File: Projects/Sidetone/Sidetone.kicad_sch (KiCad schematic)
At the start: 53 parts, among them Q1 2N3904, Q2 2N3904, Q3 2N3904, SW1 morse key, SW2 On/off, U1 4N35, U2 LM324, U3 LM386

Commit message: 20240216
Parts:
- C1, C10, C11, C12, C13, C14, C2, C3, C4, C5, C6, C7, C8, C9: footprint Capacitor_THT:CP_Radial_D8.0mm_P3.80mm -> (none)
- R1, R10, R11, R12, R13, R14, R15, R16, R17, R18, R19, R2, R20, R21, R22, R23, R24, R3, R4, R5, R6, R7, R8, R9: footprint Resistor_THT:R_Axial_DIN0207_L6.3mm_D2.5mm_P7.62mm_Horizontal -> (none)

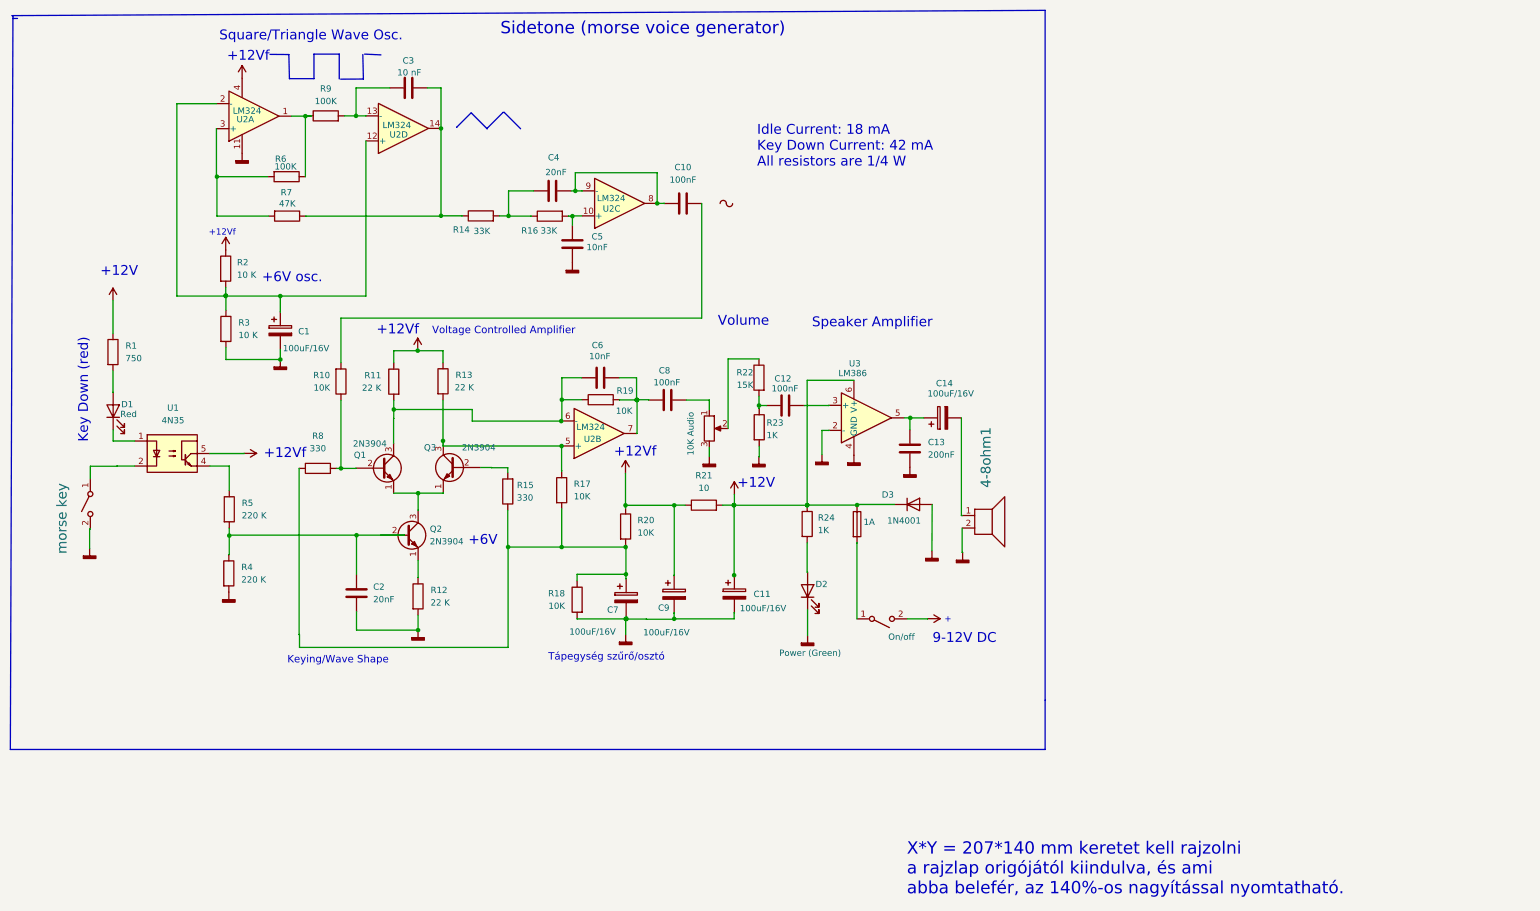
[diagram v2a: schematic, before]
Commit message: modified sidetone schematic
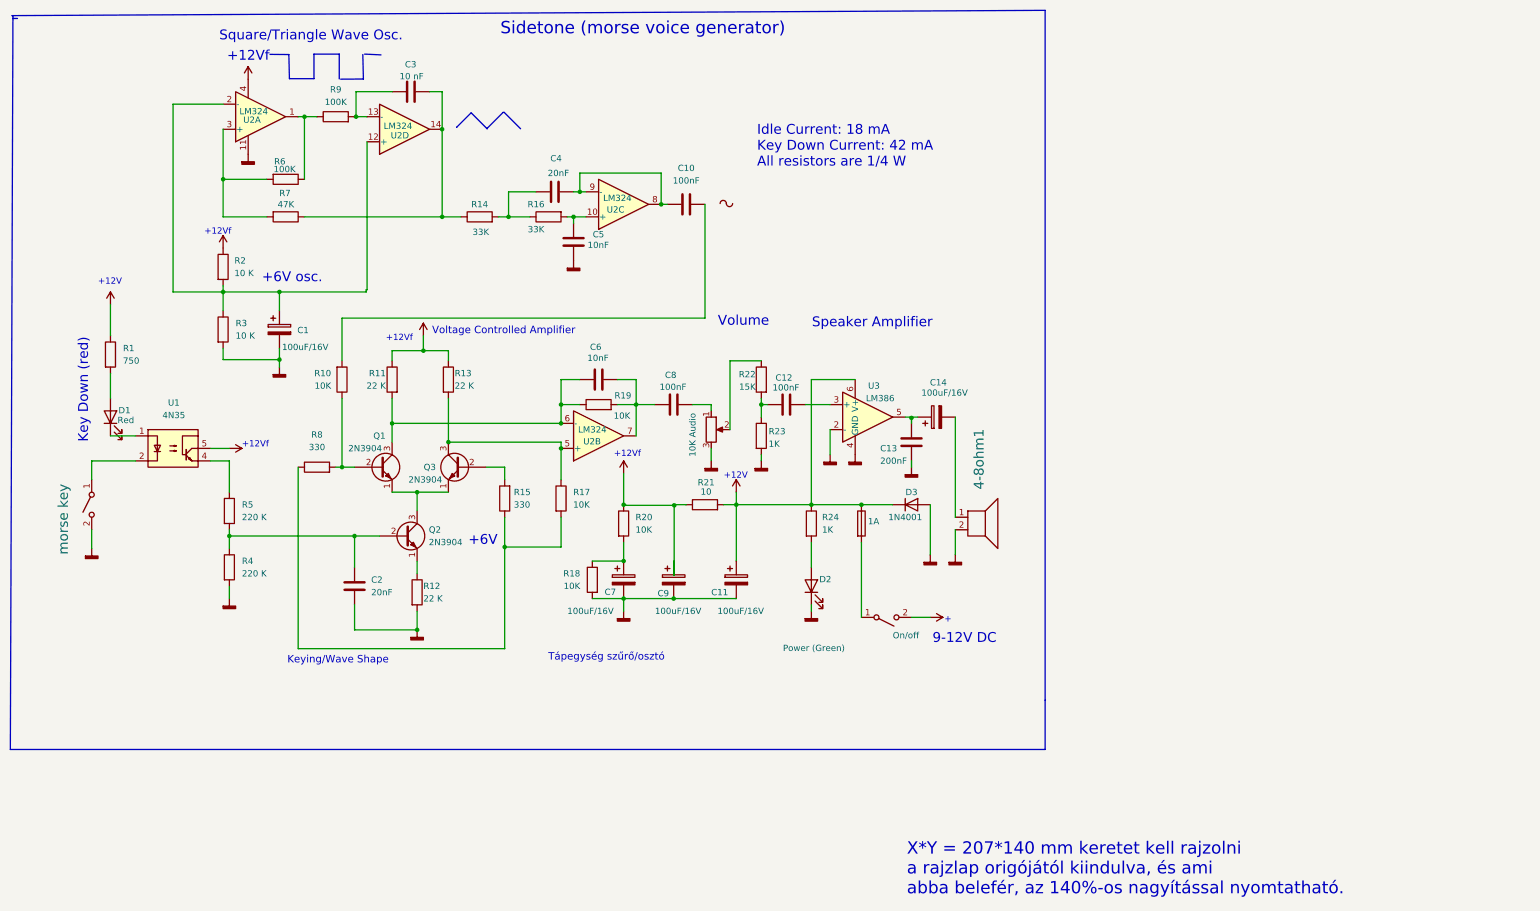
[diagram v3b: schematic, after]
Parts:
- 4-8ohm1: footprint (none) -> 000_Other_Device:Hangszoro
- C1, C11, C14, C7, C9: footprint (none) -> 000_Capacitor:CP_Radial_Elektrolit_D8.0mm_P4.0mm_H12
- C10, C12, C13, C2, C3, C4, C5, C6, C8: footprint (none) -> 000_Capacitor:C_Radial_Ceramic_D4.5mm_P5.00mm
- D1, D2: footprint (none) -> 000_Diode:LED_D5.0mm_P5.0_Clear
- D3: footprint Diode_THT:D_DO-41_SOD81_P10.16mm_Horizontal -> 000_Resistor:R_Axial_L6.3mm_D2.5mm_P10.0mm_Horizontal
- F1: footprint Fuse:Fuse_Littelfuse-LVR125 -> 000_Other_Device:Fuseholder_22x10mm_Horizontal
- Q1, Q2, Q3: footprint Package_TO_SOT_THT:TO-92_Inline -> 000_Resistor:R_Axial_L6.3mm_D2.5mm_P10.0mm_Horizontal
- R1, R10, R11, R12, R13, R14, R15, R16, R17, R18, R19, R2, R20, R21, R22, R23, R24, R3, R4, R5, R6, R7, R8, R9: footprint (none) -> 000_Resistor:R_Axial_L6.3mm_D2.5mm_P10.0mm_Horizontal
- RV1: footprint Potentiometer_THT:Potentiometer_Alps_RK09K_Single_Horizontal -> 000_Resistor:Potenciometer_4Pin_P7mm
- SW1: footprint (none) -> 000_Other_Device:Morse_Key_Pad_Group_2Pin_P7mm
- SW2: footprint (none) -> 000_Other_Device:Kapcsolo_Pad_Group_2Pin_P7mm
- U1: footprint Package_DIP:DIP-6_W7.62mm_Socket_LongPads -> 000_IC:DIP-6_W7.62mm_LongPads
- U2: footprint 001_user_library:DIP-14_296_ELL_LM324 -> 000_IC:DIP-14_LM324
- U3: footprint Package_DIP:DIP-6_W7.62mm_LongPads -> 000_IC:DIP-8_W7.62mm_Socket_LongPads
- V1: footprint 001_user_library:DIP-14_296_ELL_LM324 -> (none)
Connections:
- net at C7.1, R18.1, R20.2: no longer R15.1, R17.2, R8.1
- new net: R15.1, R17.2, R8.1
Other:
- moved on the sheet: 4-8ohm1, C10, C11, C13, C14, C2, C3, C4, C6, C7, C8, C9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

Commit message: 18-2
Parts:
- removed V1: VSIN, symbol Simulation_SPICE:VSIN
- Q1, Q2, Q3: footprint 000_Resistor:R_Axial_L6.3mm_D2.5mm_P10.0mm_Horizontal -> 000_Transistor:TO-92_Kis_Muanyag_Hazas_Transistor

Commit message: 20240222
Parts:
- added GND1: ~, 000_Other_Device:GND, symbol 000_Device:GND
- added Vcc1: ~, 000_Other_Device:+Vcc, symbol 000_Device:Vcc
- renumbered R5 to R4, R4 to R5
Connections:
- net GNDD: now also GND1. (GND)
- net VCC: now also Vcc1.
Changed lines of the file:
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@@
+    (stroke (width 0) (type default))
+  )
+  (wire (pts (xy 147.32 100.33) (xy 162.56 100.33))
     (stroke (width 0) (type default))
   )
@@
     (stroke (width 0) (type default))
   )
+  (wire (pts (xy 186.69 100.33) (xy 186.69 110.49))
+    (stroke (width 0) (type default))
+  )
   (polyline (pts (xy 158.934 42.4225) (xy 160.8121 42.4523))
     (stroke (width 0) (type default))
@@
   )
   (polyline (pts (xy 96.7546 23.9506) (xy 99.9939 20.7113))
-    (stroke (width 0) (type default))
-  )
-  (wire (pts (xy 147.32 100.33) (xy 162.56 100.33))
     (stroke (width 0) (type default))
   )
@@
   )
   (polyline (pts (xy 56.5208 8.9674) (xy 56.6364 13.8676))
-    (stroke (width 0) (type default))
-  )
-  (wire (pts (xy 186.69 100.33) (xy 186.69 110.49))
     (stroke (width 0) (type default))
   )
@@
     (effects (font (size 2 2)) (justify left bottom))
   )
-  (text "9-12V DC" (at 194.31 121.92 0)
+  (text "9-12V DC" (at 196.85 121.92 0)
     (effects (font (size 1.5 1.5) (color 0 72 72 1)) (justify left bottom))
   )
-  (text "+" (at 191.77 121.92 0)
+  (text "+" (at 194.31 121.92 0)
     (effects (font (size 1.27 1.27)) (justify left bottom))
   )
@@
         (path "/46ab649f-28d0-48e9-b5ab-0d60c8500dfe"
           (reference "R18") (unit 1)
+        )
+      )
+    )
+  )
+  (symbol (lib_id "000_Device:Vcc") (at 172.72 100.33 90) (unit 1)
+    (in_bom yes) (on_board yes) (dnp no)
+    (property "Reference" "Vcc1" (at 172.72 92.71 0)
+      (effects (font (size 1.27 1.27)) (justify right))
+    )
+    (property "Value" "~" (at 172.72 100.33 0)
+      (effects (font (size 1.27 1.27)))
+    )
+    (property "Footprint" "000_Other_Device:+Vcc" (at 172.72 100.33 0)
+      (effects (font (size 1.27 1.27)) hide)
+    )
+    (property "Datasheet" "" (at 172.72 100.33 0)
+      (effects (font (size 1.27 1.27)) hide)
+    )
+    (pin "")
+    (instances
+      (project "Sidetone"
+        (path "/46ab649f-28d0-48e9-b5ab-0d60c8500dfe"
+          (reference "Vcc1") (unit 1)
         )
       )
@@
     )
   )
+  (symbol (lib_id "000_Device:GND") (at 162.56 129.54 180) (unit 1)
+    (in_bom yes) (on_board yes) (dnp no) (fields_autoplaced)
+    (property "Reference" "GND1" (at 157.48 125.73 0)
+      (effects (font (size 1.27 1.27)) hide)
+    )
+    (property "Value" "~" (at 162.56 129.54 0)
+      (effects (font (size 1.27 1.27)))
+    )
+    (property "Footprint" "000_Other_Device:GND" (at 162.56 129.54 0)
+      (effects (font (size 1.27 1.27)) hide)
+    )
+    (property "Datasheet" "" (at 162.56 129.54 0)
+      (effects (font (size 1.27 1.27)) hide)
+    )
+    (pin "")
+    (instances
+      (project "Sidetone"
+        (path "/46ab649f-28d0-48e9-b5ab-0d60c8500dfe"
+          (reference "GND1") (unit 1)
+        )
+      )
+    )
+  )
   (symbol (lib_id "power:GNDD") (at 16.51 109.22 0) (unit 1)
     (in_bom yes) (on_board yes) (dnp no) (fields_autoplaced)
@@
   (symbol (lib_id "power:GNDD") (at 44.45 119.38 0) (unit 1)
     (in_bom yes) (on_board yes) (dnp no) (fields_autoplaced)
-    (property "Reference" "#PWR04" (at 44.45 125.73 0)
+    (property "Reference" "#PWR05" (at 44.45 125.73 0)
       (effects (font (size 1.27 1.27)) hide)
     )
@@
       (project "Sidetone"
         (path "/46ab649f-28d0-48e9-b5ab-0d60c8500dfe"
-          (reference "#PWR04") (unit 1)
+          (reference "#PWR05") (unit 1)
         )
       )
@@
   (symbol (lib_id "power:GNDD") (at 191.77 110.49 0) (unit 1)
     (in_bom yes) (on_board yes) (dnp no) (fields_autoplaced)
-    (property "Reference" "#PWR023" (at 191.77 116.84 0)
+    (property "Reference" "#PWR022" (at 191.77 116.84 0)
       (effects (font (size 1.27 1.27)) hide)
     )
@@
       (project "Sidetone"
         (path "/46ab649f-28d0-48e9-b5ab-0d60c8500dfe"
-          (reference "#PWR023") (unit 1)
+          (reference "#PWR022") (unit 1)
         )
       )
@@
   (symbol (lib_name "VCC_1") (lib_id "power:VCC") (at 44.45 88.9 270) (unit 1)
     (in_bom yes) (on_board yes) (dnp no) (fields_autoplaced)
-    (property "Reference" "#PWR07" (at 40.64 88.9 0)
+    (property "Reference" "#PWR04" (at 40.64 88.9 0)
       (effects (font (size 1.27 1.27)) hide)
     )
@@
       (project "Sidetone"
         (path "/46ab649f-28d0-48e9-b5ab-0d60c8500dfe"
-          (reference "#PWR07") (unit 1)
+          (reference "#PWR04") (unit 1)
         )
       )
@@
   (symbol (lib_id "power:GNDD") (at 82.55 125.73 0) (unit 1)
     (in_bom yes) (on_board yes) (dnp no) (fields_autoplaced)
-    (property "Reference" "#PWR010" (at 82.55 132.08 0)
+    (property "Reference" "#PWR09" (at 82.55 132.08 0)
       (effects (font (size 1.27 1.27)) hide)
     )
@@
       (project "Sidetone"
         (path "/46ab649f-28d0-48e9-b5ab-0d60c8500dfe"
-          (reference "#PWR010") (unit 1)
+          (reference "#PWR09") (unit 1)
         )
       )
@@
   (symbol (lib_id "Device:R") (at 44.45 101.6 0) (unit 1)
     (in_bom yes) (on_board yes) (dnp no) (fields_autoplaced)
-    (property "Reference" "R5" (at 46.99 100.33 0)
+    (property "Reference" "R4" (at 46.99 100.33 0)
       (effects (font (size 1.27 1.27)) (justify left))
     )
@@
       (project "Sidetone"
         (path "/46ab649f-28d0-48e9-b5ab-0d60c8500dfe"
-          (reference "R5") (unit 1)
+          (reference "R4") (unit 1)
         )
       )
@@
   (symbol (lib_id "power:VCC") (at 198.12 123.19 270) (unit 1)
     (in_bom yes) (on_board yes) (dnp no) (fields_autoplaced)
-    (property "Reference" "#PWR021" (at 194.31 123.19 0)
+    (property "Reference" "#PWR023" (at 194.31 123.19 0)
       (effects (font (size 1.27 1.27)) hide)
     )
@@
       (project "Sidetone"
         (path "/46ab649f-28d0-48e9-b5ab-0d60c8500dfe"
-          (reference "#PWR021") (unit 1)
+          (reference "#PWR023") (unit 1)
         )
       )
@@
   (symbol (lib_id "power:PWR_FLAG") (at 193.04 123.19 180) (unit 1)
     (in_bom yes) (on_board yes) (dnp no) (fields_autoplaced)
-    (property "Reference" "#FLG01" (at 193.04 125.095 0)
+    (property "Reference" "#FLG02" (at 193.04 125.095 0)
       (effects (font (size 1.27 1.27)) hide)
     )
@@
       (project "Sidetone"
         (path "/46ab649f-28d0-48e9-b5ab-0d60c8500dfe"
-          (reference "#FLG01") (unit 1)
+          (reference "#FLG02") (unit 1)
         )
       )
@@
   (symbol (lib_id "power:VCC") (at 48.26 13.97 0) (unit 1)
     (in_bom yes) (on_board yes) (dnp no) (fields_autoplaced)
-    (property "Reference" "#PWR05" (at 48.26 17.78 0)
+    (property "Reference" "#PWR06" (at 48.26 17.78 0)
       (effects (font (size 1.27 1.27)) hide)
     )
@@
       (project "Sidetone"
         (path "/46ab649f-28d0-48e9-b5ab-0d60c8500dfe"
-          (reference "#PWR05") (unit 1)
+          (reference "#PWR06") (unit 1)
         )
       )
@@
   (symbol (lib_id "Device:R") (at 44.45 113.03 0) (unit 1)
     (in_bom yes) (on_board yes) (dnp no) (fields_autoplaced)
-    (property "Reference" "R4" (at 46.99 111.76 0)
+    (property "Reference" "R5" (at 46.99 111.76 0)
       (effects (font (size 1.27 1.27)) (justify left))
     )
@@
       (project "Sidetone"
         (path "/46ab649f-28d0-48e9-b5ab-0d60c8500dfe"
-          (reference "R4") (unit 1)
+          (reference "R5") (unit 1)
         )
       )
@@
   (symbol (lib_id "power:GNDD") (at 48.26 29.21 0) (unit 1)
     (in_bom yes) (on_board yes) (dnp no) (fields_autoplaced)
-    (property "Reference" "#PWR06" (at 48.26 35.56 0)
+    (property "Reference" "#PWR07" (at 48.26 35.56 0)
       (effects (font (size 1.27 1.27)) hide)
     )
@@
       (project "Sidetone"
         (path "/46ab649f-28d0-48e9-b5ab-0d60c8500dfe"
-          (reference "#PWR06") (unit 1)
+          (reference "#PWR07") (unit 1)
         )
       )
@@
   (symbol (lib_id "power:GNDD") (at 186.69 110.49 0) (unit 1)
     (in_bom yes) (on_board yes) (dnp no) (fields_autoplaced)
-    (property "Reference" "#PWR022" (at 186.69 116.84 0)
+    (property "Reference" "#PWR021" (at 186.69 116.84 0)
       (effects (font (size 1.27 1.27)) hide)
     )
@@
       (project "Sidetone"
         (path "/46ab649f-28d0-48e9-b5ab-0d60c8500dfe"
-          (reference "#PWR022") (unit 1)
+          (reference "#PWR021") (unit 1)
         )
       )
@@
   (symbol (lib_id "power:PWR_FLAG") (at 162.56 129.54 270) (unit 1)
     (in_bom yes) (on_board yes) (dnp no) (fields_autoplaced)
-    (property "Reference" "#FLG02" (at 164.465 129.54 0)
+    (property "Reference" "#FLG01" (at 164.465 129.54 0)
       (effects (font (size 1.27 1.27)) hide)
     )
@@
       (project "Sidetone"
         (path "/46ab649f-28d0-48e9-b5ab-0d60c8500dfe"
-          (reference "#FLG02") (unit 1)
+          (reference "#FLG01") (unit 1)
         )
       )
@@
   (symbol (lib_id "power:VCC") (at 83.82 66.04 0) (unit 1)
     (in_bom yes) (on_board yes) (dnp no) (fields_autoplaced)
-    (property "Reference" "#PWR09" (at 83.82 69.85 0)
+    (property "Reference" "#PWR010" (at 83.82 69.85 0)
       (effects (font (size 1.27 1.27)) hide)
     )
@@
       (project "Sidetone"
         (path "/46ab649f-28d0-48e9-b5ab-0d60c8500dfe"
-          (reference "#PWR09") (unit 1)
-        )
-      )
+          (reference "#PWR010") (unit 1)
+        )
+      )

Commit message: building pcb 20240222
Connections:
- net VCC: no longer C11.1, C9.1, D3.1 (K), F1.1, R1.1, R11.1, R13.1, R2.1, R20.1, R21.1, R21.2, R24.1, U1.5, U2.4 (V+), U3.6 (V+), Vcc1.
- net at C6.2, C8.1, R19.2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: now also C9.1, R11.1, R13.1, R2.1, R20.1, R21.1, U1.5, U2.4 (V+)
- net at R1.2: now also C11.1, D3.1 (K), F1.1, R21.2, R24.1, U3.6 (V+), Vcc1.; no longer D1.2 (A)
- new net: D1.2 (A), R1.1
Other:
- note removed: "+12Vf"
- moved on the sheet: R1
